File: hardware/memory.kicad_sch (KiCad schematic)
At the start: 0 parts

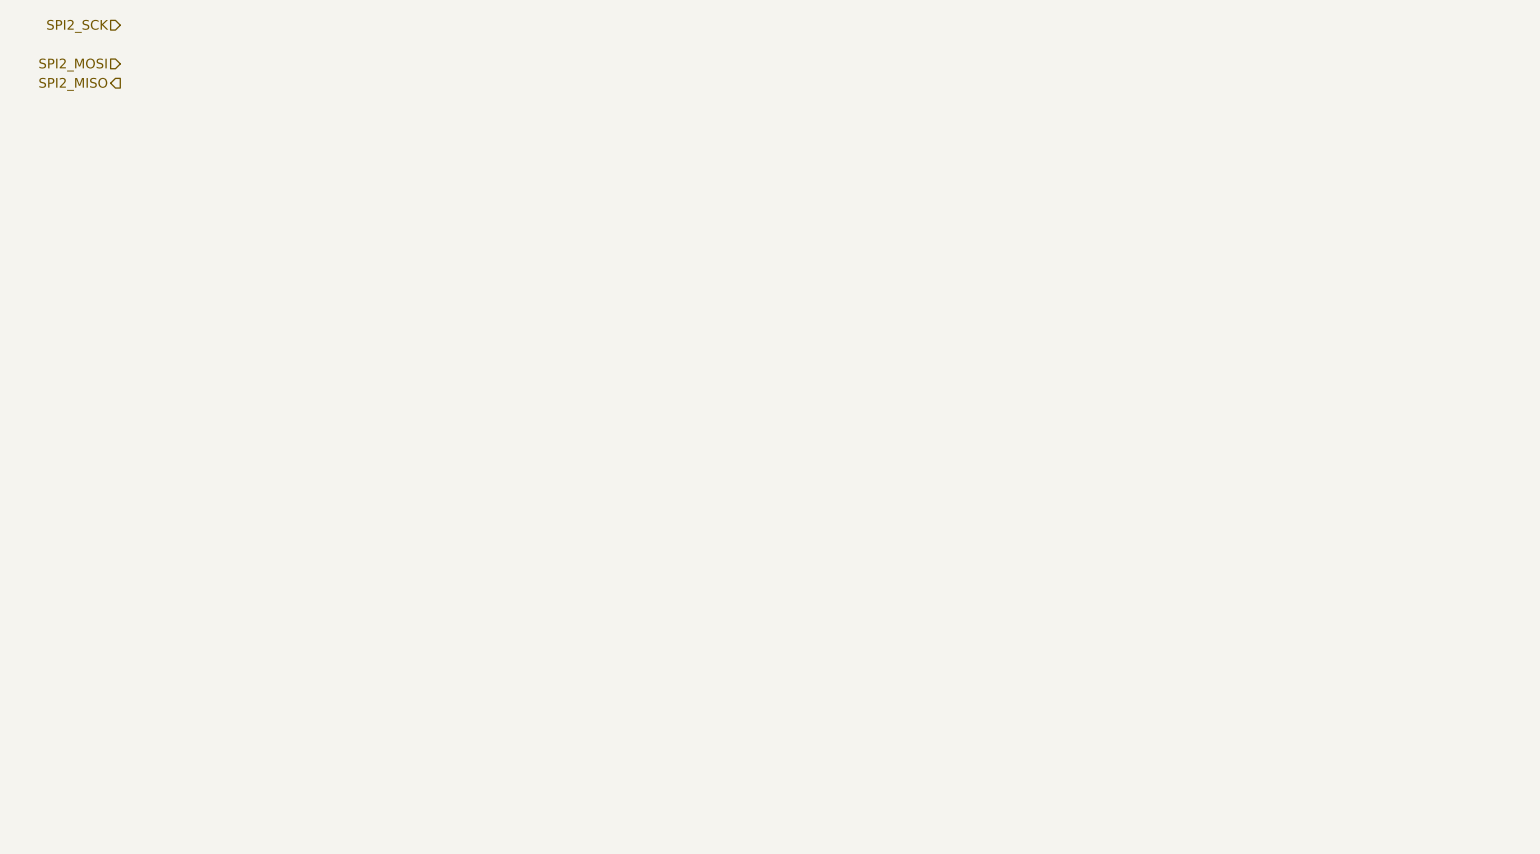
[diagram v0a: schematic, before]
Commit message: feat(kicad): Added several open sourced footprint libraries, finished schematic design for nrf, uwb, tof, flash, motors and added all reference material to refs folder
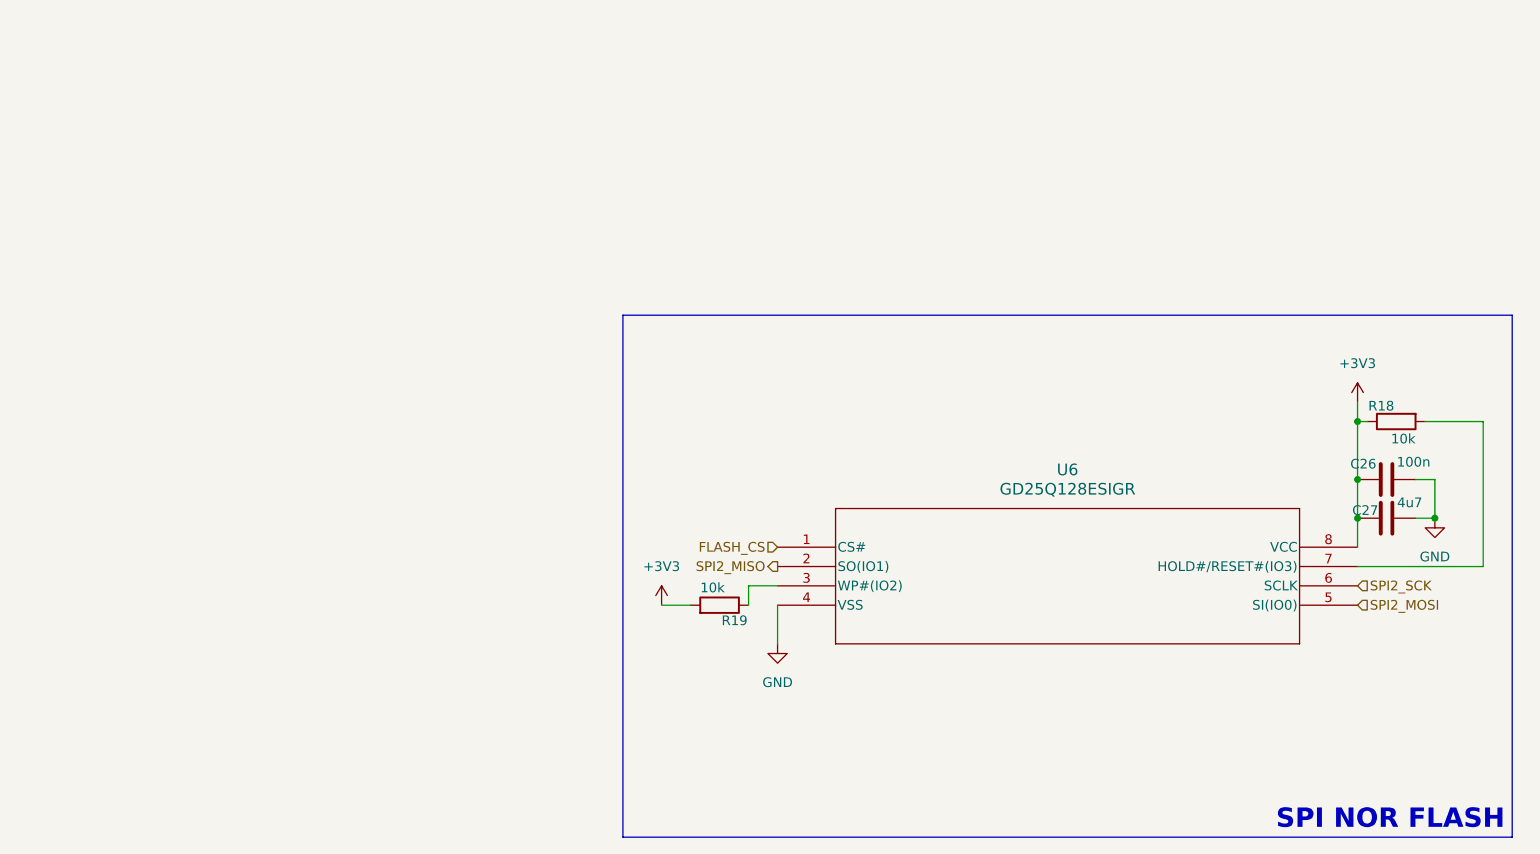
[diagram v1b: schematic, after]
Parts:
- added C26: 100n, symbol Device:C
- added C27: 4u7, symbol Device:C
- added R18, R19: 10k, symbol Device:R
- added U6: GD25Q128ESIGR, GD25Q128:SOP8_208MIL_GDV, symbol GD25Q128:GD25Q128ESIGR
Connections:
- net SPI2_MISO: now also U6.2 (SO(IO1))
- net SPI2_MOSI: now also U6.5 (SI(IO0))
- net SPI2_SCK: now also U6.6 (SCLK)
- new net: R19.1, U6.3 (WP#(IO2))
- new net: R18.2, U6.7 (HOLD#/RESET#(IO3))
- new net +3V3: C26.1, C27.1, R18.1, R19.2, U6.8 (VCC)
- new net FLASH_CS: U6.1 (CS#)
- new net GND: C26.2, C27.2, U6.4 (VSS)
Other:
- note added: "SPI NOR FLASH"
